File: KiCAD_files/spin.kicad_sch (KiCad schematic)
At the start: 41 parts, among them J1 OwnTech_SPIN, J5 FTSH-107-01-F-DV-K, J6 USB_C_Receptacle_USB2.0, SW1 Push Button, SW2 Push Button, T1 Tab, T2 Tab, T3 Tab, T4 Tab, U1 STM32G474RE, U2 AZ1117-33, U3 WE-TVS-82400102, Y1 ECS-240-8-37-CKM-TR3 - 24MHz

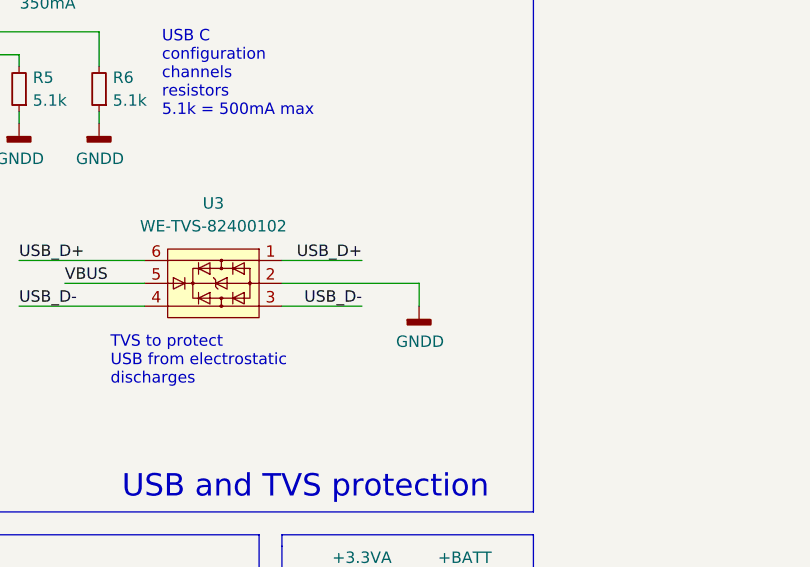
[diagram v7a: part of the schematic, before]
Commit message: added test points for D+ D- and gndd. Updated the silk to SPIN V1.1.0
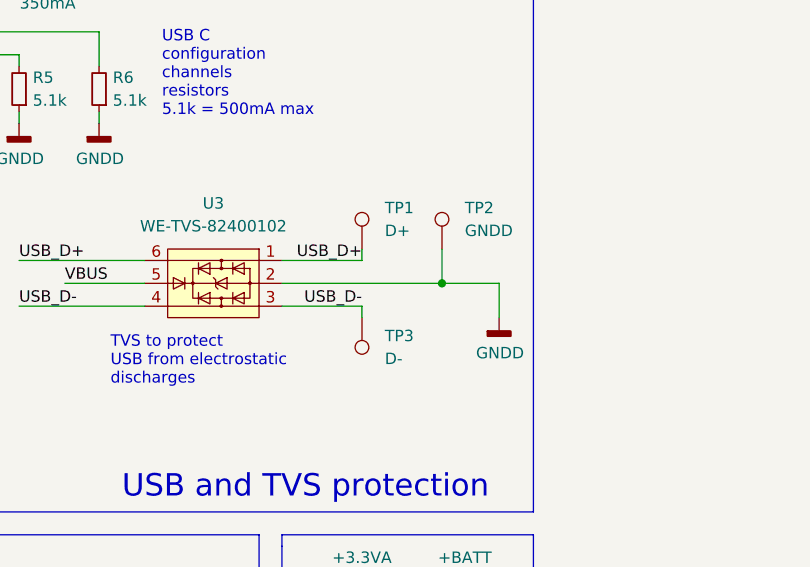
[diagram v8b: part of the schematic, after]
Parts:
- added TP1: D+, TestPoint:TestPoint_Pad_D1.0mm, symbol Connector:TestPoint
- added TP2: GNDD, TestPoint:TestPoint_Pad_D1.0mm, symbol Connector:TestPoint
- added TP3: D-, TestPoint:TestPoint_Pad_D1.0mm, symbol Connector:TestPoint
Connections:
- net GNDD: now also TP2.1
- net USB_D+: now also TP1.1
- net USB_D-: now also TP3.1
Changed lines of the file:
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@@
   (junction (at 351.79 118.11) (diameter 0) (color 0 0 0 0)
   )
+  (junction (at 396.24 74.93) (diameter 0) (color 0 0 0 0)
+  )
   (junction (at 97.79 50.8) (diameter 0) (color 0 0 0 0)
   )
@@
     (stroke (width 0) (type default))
   )
+  (wire (pts (xy 387.35 77.47) (xy 387.35 78.74))
+    (stroke (width 0) (type default))
+  )
   (wire (pts (xy 256.54 109.22) (xy 267.97 109.22))
     (stroke (width 0) (type default))
@@
     (stroke (width 0) (type default))
   )
+  (wire (pts (xy 387.35 71.12) (xy 387.35 72.39))
+    (stroke (width 0) (type default))
+  )
   (wire (pts (xy 354.33 74.93) (xy 363.22 74.93))
     (stroke (width 0) (type default))
@@
     (stroke (width 0) (type default))
   )
+  (wire (pts (xy 396.24 74.93) (xy 378.46 74.93))
+    (stroke (width 0) (type default))
+  )
   (wire (pts (xy 349.25 77.47) (xy 363.22 77.47))
     (stroke (width 0) (type default))
@@
     (stroke (width 0) (type default))
   )
-  (wire (pts (xy 393.7 77.47) (xy 393.7 74.93))
+  (wire (pts (xy 402.59 78.74) (xy 402.59 74.93))
     (stroke (width 0) (type default))
   )
@@
     (stroke (width 0) (type default))
   )
-  (wire (pts (xy 393.7 74.93) (xy 378.46 74.93))
+  (wire (pts (xy 402.59 74.93) (xy 396.24 74.93))
     (stroke (width 0) (type default))
   )
@@
     (stroke (width 0) (type default))
   )
+  (wire (pts (xy 396.24 71.12) (xy 396.24 74.93))
+    (stroke (width 0) (type default))
+  )
   (wire (pts (xy 177.8 86.36) (xy 194.31 86.36))
     (stroke (width 0) (type default))
@@
     )
   )
+  (symbol (lib_id "Connector:TestPoint") (at 387.35 71.12 0) (unit 1)
+    (in_bom yes) (on_board yes) (dnp no) (fields_autoplaced)
+    (property "Reference" "TP1" (at 389.89 66.548 0)
+      (effects (font (size 1.27 1.27)) (justify left))
+    )
+    (property "Value" "D+" (at 389.89 69.088 0)
+      (effects (font (size 1.27 1.27)) (justify left))
+    )
+    (property "Footprint" "TestPoint:TestPoint_Pad_D1.0mm" (at 392.43 71.12 0)
+      (effects (font (size 1.27 1.27)) hide)
+    )
+    (property "Datasheet" "~" (at 392.43 71.12 0)
+      (effects (font (size 1.27 1.27)) hide)
+    )
+    (pin "1")
+    (instances
+      (project "spin"
+        (path "/87c78429-be2b-40ed-8d3b-56cb9666a56f"
+          (reference "TP1") (unit 1)
+        )
+      )
+    )
+  )
   (symbol (lib_id "power:GNDD") (at 163.83 264.16 0) (unit 1)
     (in_bom yes) (on_board yes) (dnp no)
@@
     )
   )
-  (symbol (lib_id "power:GNDD") (at 393.7 77.47 0) (unit 1)
+  (symbol (lib_id "power:GNDD") (at 402.59 78.74 0) (unit 1)
     (in_bom yes) (on_board yes) (dnp no)
-    (property "Reference" "#PWR040" (at 393.7 83.82 0)
+    (property "Reference" "#PWR040" (at 402.59 85.09 0)
       (effects (font (size 1.27 1.27)) hide)
     )
-    (property "Value" "GNDD" (at 393.8016 81.407 0)
+    (property "Value" "GNDD" (at 402.6916 82.677 0)
       (effects (font (size 1.27 1.27)))
     )
-    (property "Footprint" "" (at 393.7 77.47 0)
+    (property "Footprint" "" (at 402.59 78.74 0)
       (effects (font (size 1.27 1.27)) hide)
     )
-    (property "Datasheet" "" (at 393.7 77.47 0)
+    (property "Datasheet" "" (at 402.59 78.74 0)
       (effects (font (size 1.27 1.27)) hide)
     )
@@
         )
       )
+    )
+  )
+  (symbol (lib_id "Connector:TestPoint") (at 387.35 78.74 180) (unit 1)
+    (in_bom yes) (on_board yes) (dnp no) (fields_autoplaced)
+    (property "Reference" "TP3" (at 389.89 80.772 0)
+      (effects (font (size 1.27 1.27)) (justify right))
+    )
+    (property "Value" "D-" (at 389.89 83.312 0)
+      (effects (font (size 1.27 1.27)) (justify right))
+    )
+    (property "Footprint" "TestPoint:TestPoint_Pad_D1.0mm" (at 382.27 78.74 0)
+      (effects (font (size 1.27 1.27)) hide)
+    )
+    (property "Datasheet" "~" (at 382.27 78.74 0)
+      (effects (font (size 1.27 1.27)) hide)
+    )
+    (pin "1")
+    (instances
+      (project "spin"
+        (path "/87c78429-be2b-40ed-8d3b-56cb9666a56f"
+          (reference "TP3") (unit 1)
+        )
+      )
+    )
+  )
+  (symbol (lib_id "Connector:TestPoint") (at 396.24 71.12 0) (unit 1)
+    (in_bom yes) (on_board yes) (dnp no) (fields_autoplaced)
+    (property "Reference" "TP2" (at 398.78 66.548 0)
+      (effects (font (size 1.27 1.27)) (justify left))
+    )
+    (property "Value" "GNDD" (at 398.78 69.088 0)
+      (effects (font (size 1.27 1.27)) (justify left))
+    )
+    (property "Footprint" "TestPoint:TestPoint_Pad_D1.0mm" (at 401.32 71.12 0)
+      (effects (font (size 1.27 1.27)) hide)
+    )
+    (property "Datasheet" "~" (at 401.32 71.12 0)
+      (effects (font (size 1.27 1.27)) hide)
+    )
+    (pin "1")
+    (instances
+      (project "spin"
+        (path "/87c78429-be2b-40ed-8d3b-56cb9666a56f"
+          (reference "TP2") (unit 1)
+        )
+      )
